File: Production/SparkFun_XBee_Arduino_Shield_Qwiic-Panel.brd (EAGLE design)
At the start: 120.9 x 213.4 mm, 1008 parts, among them J1 QWIIC_RIGHT_ANGLE, J13 QWIIC_RIGHT_ANGLE, J17 QWIIC_RIGHT_ANGLE, J21 QWIIC_RIGHT_ANGLE, J4 QWIIC_RIGHT_ANGLE, J9 QWIIC_RIGHT_ANGLE, Q1 220mA/50V/3.5Ω, Q11 3.1A/30V/105mΩ, Q12 220mA/50V/3.5Ω, Q13 20V/4.2A/52mΩ/1.4W, Q15 3.1A/30V/105mΩ, Q16 220mA/50V/3.5Ω, Q17 20V/4.2A/52mΩ/1.4W, Q19 3.1A/30V/105mΩ, Q2 20V/4.2A/52mΩ/1.4W, Q20 220mA/50V/3.5Ω, Q21 20V/4.2A/52mΩ/1.4W, Q23 3.1A/30V/105mΩ, Q24 220mA/50V/3.5Ω, Q3 3.1A/30V/105mΩ, Q5 20V/4.2A/52mΩ/1.4W, Q6 3.1A/30V/105mΩ, Q8 220mA/50V/3.5Ω, Q9 20V/4.2A/52mΩ/1.4W, U1 FSUSB30MUX_MSOP10, U10 FT231XS, U11 AP63203, U12 ESD Diode, U13 FSUSB30MUX_MSOP10, U14 ESD Diode, U15 FT231XS, U16 AP63203, U17 ESD Diode, U18 FSUSB30MUX_MSOP10, U19 ESD Diode, U2 AP63203, U20 FT231XS, U21 AP63203, U22 ESD Diode, U23 FSUSB30MUX_MSOP10, U24 ESD Diode, U25 FT231XS, U26 AP63203, U27 ESD Diode, U28 FSUSB30MUX_MSOP10, U29 ESD Diode, U3 ESD Diode, U30 FT231XS, U4 FT231XS, U5 ESD Diode, U6 AP63203, U7 ESD Diode, U8 FSUSB30MUX_MSOP10, U9 ESD Diode, X1 JUMPER-SMT_2_NO_SILK, X2 JUMPER-SMT_2_NO_SILK, X3 JUMPER-SMT_2_NO_SILK, X4 JUMPER-SMT_2_NO_SILK, X5 JUMPER-SMT_2_NO_SILK, X6 JUMPER-SMT_2_NO_SILK

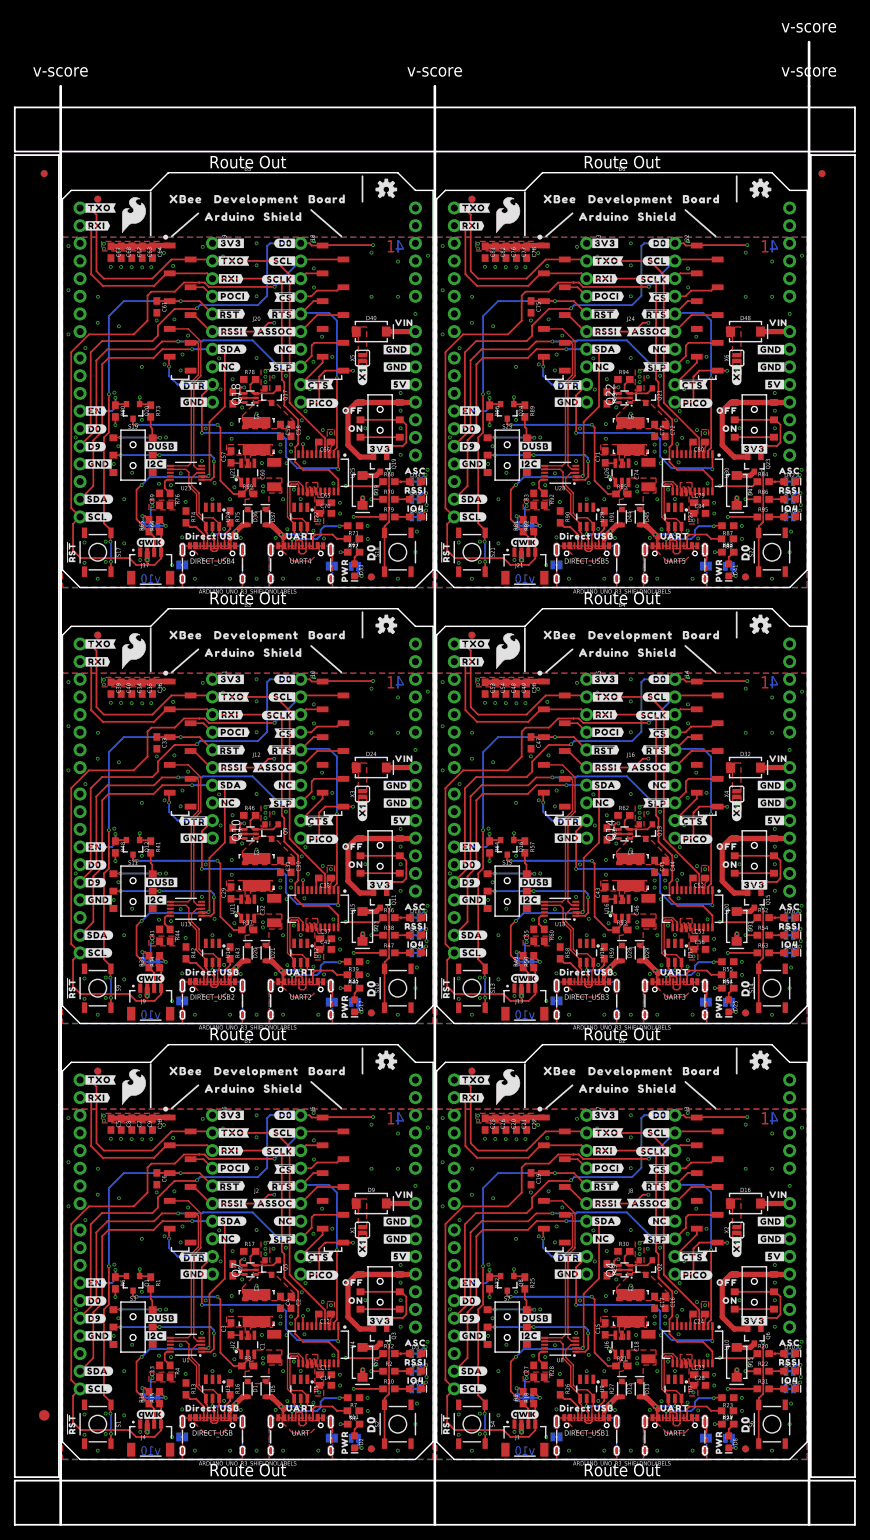
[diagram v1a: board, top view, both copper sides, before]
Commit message: Small adjustment to design file after approving proximity DRC error
* Remakes panels
* Deletes old library
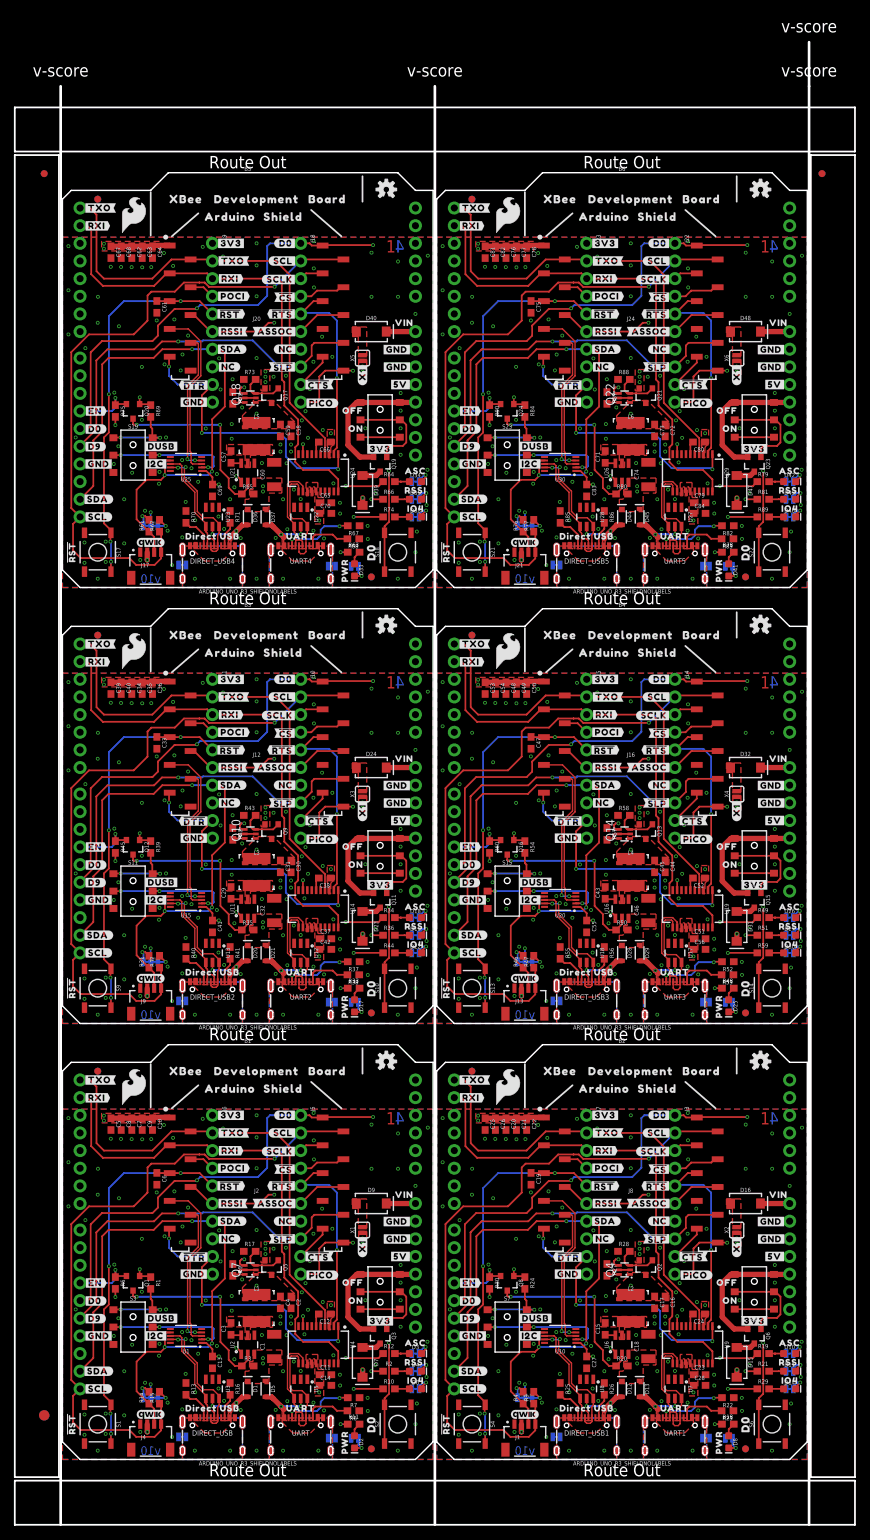
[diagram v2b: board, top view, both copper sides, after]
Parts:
- removed R91: 5.1k, SparkFun-Resistors:0603
- removed R92: 100, SparkFun-Resistors:0603
- removed R93: 100k, SparkFun-Resistors:0603
- removed R94: 1M, SparkFun-Resistors:0603
- removed R95: 330, SparkFun-Resistors:0603
- removed R96: 10k, SparkFun-Resistors:0603
- R18, R33: value 2.2k -> 4.7k
- R19, R51: value 4.7k -> 2.2k
- R20, R50, R54, R65, R84: value 2.2k -> 100k
- R21, R61, R77: value 100k -> 2.2k
- R22, R38, R52, R68, R70, R82, R86: value 2.2k -> 5.1k
- R24, R27, R39, R42, R72, R87: value 5.1k -> 100k
- R25, R37, R41, R53, R85: value 100k -> 5.1k
- R28: value 100 -> 1M
- R29, R89: value 100k -> 330
- R30: value 1M -> 10k
- R31, R47, R79: value 330 -> 2.2k
- R32, R64: value 10k -> 2.2k
- R35: value 4.7k -> 100k
- R4, R76: value 100 -> 2.2k
- R43, R58, R88: value 5.1k -> 1M
- R44: value 100 -> 330
- R45: value 100k -> 10k
- R46, R62: value 1M -> 2.2k
- R48: value 10k -> 4.7k
- R59, R74: value 5.1k -> 330
- R60: value 100 -> 10k
- R63: value 330 -> 4.7k
- R67, R83: value 4.7k -> 5.1k
- R73: value 100k -> 1M
- R75, R90: value 5.1k -> 10k
- R78: value 1M -> 4.7k
- R80: value 10k -> 100k
- U1: value FSUSB30MUX_MSOP10 -> FSUSB42MUX
- U10, U15, U20, U25, U30: value FT231XS -> FSUSB42MUX; device SparkFun-IC-Comms:SSOP20_L -> SparkFun-IC-Special-Function:MSOP10
- U13, U18, U23, U28, U8: value FSUSB30MUX_MSOP10 -> ESD Diode; device SparkFun-IC-Special-Function:MSOP10 -> SparkFun-DiscreteSemi:SOT-23-6
- U14, U19, U24, U29, U9: value ESD Diode -> FT231XS; device SparkFun-DiscreteSemi:SOT-23-6 -> SparkFun-IC-Comms:SSOP20_L
- moved R31 107.7 mm to (12.4, 71.6), turned to 90 degrees
- moved R48 90.5 mm to (95.8, 67.8), turned to 0 degrees
- moved R63 82.4 mm to (41.9, 130.6)
- moved R61 79.4 mm to (12.4, 134.4), turned to 90 degrees
- moved R62 78.8 mm to (14.0, 134.4), turned to 90 degrees
- moved R80 73.9 mm to (80.5, 138.9), turned to 0 degrees
- moved R78 73.2 mm to (95.8, 130.6)
- moved R32 66.3 mm to (14.0, 71.6), turned to 90 degrees
- moved R64 54.5 mm to (47.0, 140.7), turned to 0 degrees
- moved R79 54.1 mm to (100.8, 140.7)
- moved R4 50.9 mm to (66.3, 8.89), turned to 90 degrees
- moved R76 50.9 mm to (66.3, 134.4), turned to 90 degrees
- moved R77 47.0 mm to (67.8, 134.4), turned to 90 degrees
- moved R46 44.6 mm to (66.3, 71.6), turned to 90 degrees
- moved R89 37.5 mm to (100.8, 135.6), turned to 0 degrees
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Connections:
- removed net N$102 (its old number): DIRECT_USB4.A5, R74.2
- removed net N$103 (its old number): R76.1, U23.10
- removed net N$104 (its old number): Q18.2, Q18.5, Q18.6, R77.2
- removed net N$105 (its old number): Q17.1, Q18.3, R78.2
- removed net N$111 (its old number): I2C_PU5.3, R81.2
- removed net N$112 (its old number): I2C_PU5.1, R82.2
- removed net N$113 (its old number): D41.A, R83.2
- removed net N$123 (its old number): DIRECT_USB5.B5, R91.2
- removed net N$124 (its old number): DIRECT_USB5.A5, R90.2
- removed net N$125 (its old number): R92.1, U28.10
- removed net N$126 (its old number): Q22.2, Q22.5, Q22.6, R93.2
- removed net N$127: Q21.1, Q22.3, R94.2
- removed net N$128: D46.A, R95.2
- removed net N$25 (its old number): D10.A, R20.2
- removed net N$31 (its old number): D11.A, R22.2
- removed net N$39 (its old number): Q2.1, Q4.3, R30.2
- removed net N$40 (its old number): D14.A, R31.2
- removed net N$47 (its old number): D17.A, R35.2
- removed net N$48 (its old number): D18.A, R36.2
- removed net N$60 (its old number): Q10.2, Q10.5, Q10.6, R45.2
- removed net N$61 (its old number): Q10.3, Q9.1, R46.2
- removed net N$62 (its old number): D22.A, R47.2
- removed net N$68 (its old number): I2C_PU3.1, R50.2
- removed net N$69 (its old number): D25.A, R51.2
- removed net N$70 (its old number): D26.A, R52.2
- removed net N$81 (its old number): R60.1, U18.10
- removed net N$82 (its old number): Q14.2, Q14.5, Q14.6, R61.2
- removed net N$83 (its old number): Q13.1, Q14.3, R62.2
- removed net N$84 (its old number): D30.A, R63.2
- removed net N$89 (its old number): I2C_PU4.3, R65.2
- removed net N$90 (its old number): I2C_PU4.1, R66.2
- removed net N$91 (its old number): D33.A, R67.2
- removed net N$92 (its old number): D34.A, R68.2
- new net N$107: I2C_PU5.1, R77.2
- new net N$108: D41.A, R78.2
- new net N$109: D42.A, R79.2
- new net N$116: R83.2, UART5.B5
- new net N$117: R82.2, UART5.A5
- new net N$118: DIRECT_USB5.B5, R86.2
- new net N$120: Q22.2, Q22.5, Q22.6, R87.2
- new net N$30: D11.A, R21.2
- new net N$32: R23.2, UART1.B5
- new net N$43: I2C_PU2.3, R31.2
- new net N$44: I2C_PU2.1, R32.2
- new net N$51: D19.A, R36.2
- new net N$54: R37.2, UART2.A5
- new net N$64: I2C_PU3.3, R46.2
- new net N$65: I2C_PU3.1, R47.2
- new net N$66: D25.A, R48.2
- new net N$72: D27.A, R51.2
- new net N$74: R53.2, UART3.B5
- new net N$76: DIRECT_USB3.B5, R56.2
- new net N$85: I2C_PU4.3, R61.2
- new net N$86: I2C_PU4.1, R62.2
- new net N$87: D33.A, R63.2
- new net N$88: D34.A, R64.2
- new net N$93: D35.A, R66.2
- new net N$95: R68.2, UART4.B5
- new net N$96: R67.2, UART4.A5
- new net N$98: DIRECT_USB4.A5, R70.2
- net 3.3V: now also U1.1; no longer R4.2
- net 3.3V1: now also R18.1, R24.1, R30.2, U10.1, U9.13, U9.14, U9.15, U9.3; no longer R19.1, R25.1, R28.2, R32.2, U10.13, U10.14, U10.15, U10.3
- net 3.3V2: now also R33.1, R39.1, R45.2, U14.13, U14.14, U14.15, U14.3, U15.1; no longer R35.1, R41.1, R44.2, R48.2, U15.13, U15.14, U15.15, U15.3
- net 3.3V3: now also R48.1, R54.1, U19.13, U19.14, U19.15, U19.3, U20.1; no longer R51.1, R57.1, R64.2, U20.13, U20.14, U20.15, U20.3
- net 3.3V4: now also R63.1, R69.1, R75.2, U24.13, U24.14, U24.15, U24.3, U25.1; no longer R67.1, R73.1, R76.2, R80.2, U25.13, U25.14, U25.15, U25.3
- net 3.3V5: now also R78.1, R84.1, R90.2, U29.13, U29.14, U29.15, U29.3, U30.1; no longer R83.1, R89.1, R92.2, R96.2, U30.13, U30.14, U30.15, U30.3
- net D+1: now also U9.11; no longer U10.11
- net D+2: now also U14.11; no longer U15.11
- net D+3: now also U19.11; no longer U20.11
- net D+4: now also U24.11; no longer U25.11
- net D+5: now also U29.11; no longer U30.11
- net D-1: now also U9.12; no longer U10.12
- net D-2: now also U14.12; no longer U15.12
- net D-3: now also U19.12; no longer U20.12
- net D-4: now also U24.12; no longer U25.12
- net D-5: now also U29.12; no longer U30.12
- net D1/SCL1: now also R9.1; no longer R18.1
- net D1/SCL2: now also R32.1; no longer R34.1
- net D1/SCL3: now also R47.1; no longer R50.1
- net D1/SCL4: now also R62.1; no longer R66.1
- net D1/SCL5: now also R77.1; no longer R82.1
- net D10/RSSI_PWM1: now also R21.1; no longer R22.1
- net D10/RSSI_PWM2: now also R36.1; no longer R38.1
- net D10/RSSI_PWM3: now also R51.1; no longer R54.1
- net D10/RSSI_PWM4: now also R66.1; no longer R70.1
- net D10/RSSI_PWM5: now also R81.1; no longer R86.1
- net D11/SDA: now also U1.7; no longer U1.2
- net D11/SDA1: now also R4.1, U10.7; no longer R9.1, U8.2
- net D11/SDA2: now also R31.1, U15.7; no longer R33.1, U13.2
- net D11/SDA3: now also R46.1, U20.7; no longer R49.1, U18.2
- net D11/SDA4: now also R61.1, U25.7; no longer R65.1, U23.2
- net D11/SDA5: now also R76.1, U30.7; no longer R81.1, U28.2
- net D13/TXO1: now also U9.4; no longer U10.4
- net D13/TXO2: now also U14.4; no longer U15.4
- net D13/TXO3: now also U19.4; no longer U20.4
- net D13/TXO4: now also U24.4; no longer U25.4
- net D13/TXO5: now also U29.4; no longer U30.4
- net D14/RXI1: now also U9.20; no longer U10.20
- net D14/RXI2: now also U14.20; no longer U15.20
- net D14/RXI3: now also U19.20; no longer U20.20
- net D14/RXI4: now also U24.20; no longer U25.20
- net D14/RXI5: now also U29.20; no longer U30.20
- net D4/SPI_PICO1: now also R29.1; no longer R31.1
- net D4/SPI_PICO2: now also R44.1; no longer R47.1
- net D4/SPI_PICO3: now also R59.1; no longer R63.1
- net D4/SPI_PICO4: now also R74.1; no longer R79.1
- net D4/SPI_PICO5: now also R89.1; no longer R95.1
- net D5/ASSOCIATE1: now also R19.1; no longer R20.1
- net D5/ASSOCIATE2: now also R34.1; no longer R36.1
- net D5/ASSOCIATE3: now also R49.1; no longer R52.1
- net D5/ASSOCIATE4: now also R64.1; no longer R68.1
- net D5/ASSOCIATE5: now also R79.1; no longer R84.1
- net D6/!RTS!1: now also U9.2; no longer U10.2
- net D6/!RTS!2: now also U14.2; no longer U15.2
- net D6/!RTS!3: now also U19.2; no longer U20.2
- net D6/!RTS!4: now also U24.2; no longer U25.2
- net D6/!RTS!5: now also U29.2; no longer U30.2
- net D7/!CTS!1: now also U9.9; no longer U10.9
- net D7/!CTS!2: now also U14.9; no longer U15.9
- net D7/!CTS!3: now also U19.9; no longer U20.9
- net D7/!CTS!4: now also U24.9; no longer U25.9
- net D7/!CTS!5: now also U29.9; no longer U30.9
- net D8/!DTR!1: now also U9.1; no longer U10.1
- net D8/!DTR!2: now also U14.1; no longer U15.1
- net D8/!DTR!3: now also U19.1; no longer U20.1
- net D8/!DTR!4: now also U24.1; no longer U25.1
- net D8/!DTR!5: now also U29.1; no longer U30.1
- net DIRECT_D+: now also U1.9; no longer U1.3
- net DIRECT_D+1: now also U10.9, U8.6; no longer U8.3, U9.6
- net DIRECT_D+2: now also U13.6, U15.9; no longer U13.3, U14.6
- net DIRECT_D+3: now also U18.6, U20.9; no longer U18.3, U19.6
- net DIRECT_D+4: now also U23.6, U25.9; no longer U23.3, U24.6
- net DIRECT_D+5: now also U28.6, U30.9; no longer U28.3, U29.6
- net DIRECT_D-: now also U1.8; no longer U1.7
- net DIRECT_D-1: now also U10.8, U8.4; no longer U8.7, U9.4
- net DIRECT_D-2: now also U13.4, U15.8; no longer U13.7, U14.4
- net DIRECT_D-3: now also U18.4, U20.8; no longer U18.7, U19.4
- net DIRECT_D-4: now also U23.4, U25.8; no longer U23.7, U24.4
- net DIRECT_D-5: now also U28.4, U30.8; no longer U28.7, U29.4
- net DIRECT_SELECT: now also U1.2; no longer U1.1
- net DIRECT_SELECT1: now also U10.2; no longer U8.1
- net DIRECT_SELECT2: now also U15.2; no longer U13.1
- net DIRECT_SELECT3: now also U20.2; no longer U18.1
- net DIRECT_SELECT4: now also U25.2; no longer U23.1
- net DIRECT_SELECT5: now also U30.2; no longer U28.1
- net DIRECT_USB1: now also R24.2; no longer R25.2
- net DIRECT_USB2: now also R39.2; no longer R41.2
- net DIRECT_USB3: now also R54.2; no longer R57.2
- net DIRECT_USB4: now also R69.2; no longer R73.2
- net DIRECT_USB5: now also R84.2; no longer R89.2
- net EN-TRANS1: now also R30.1; no longer R32.1
- net EN-TRANS2: now also R45.1; no longer R48.1
- net EN-TRANS3: now also R60.1; no longer R64.1
- net EN-TRANS4: now also R75.1; no longer R80.1
- net EN-TRANS5: now also R90.1; no longer R96.1
- net EN1: now also R20.1; no longer R21.1
- net EN2: now also R35.1; no longer R37.1
- net EN3: now also R50.1; no longer R53.1
- net EN4: now also R65.1; no longer R69.1
- net EN5: now also R80.1; no longer R85.1
- net GND: now also U1.10; no longer U1.9
- net GND1: now also R22.1, R25.1, R28.1, U10.10, U10.5, U8.2, U9.16, U9.6; no longer R24.1, R29.1, R30.1, U10.16, U10.6, U8.5, U8.9, U9.2
- net GND2: now also R37.1, R38.1, R41.1, U13.2, U14.16, U14.6, U15.10, U15.5; no longer R39.1, R45.1, R46.1, U13.5, U13.9, U14.2, U15.16, U15.6
- net GND3: now also R52.1, R53.1, R57.1, U18.2, U19.16, U19.6, U20.10, U20.5; no longer R59.1, R61.1, R62.1, U18.5, U18.9, U19.2, U20.16, U20.6
- net GND4: now also R67.1, R68.1, R70.1, R73.1, U23.2, U24.16, U24.6, U25.10, U25.5; no longer R74.1, R75.1, R77.1, R78.1, U23.5, U23.9, U24.2, U25.16, U25.6
- net GND5: now also R82.1, R83.1, R85.1, R86.1, U28.2, U29.16, U29.6, U30.10, U30.5; no longer R90.1, R91.1, R93.1, R94.1, U28.5, U28.9, U29.2, U30.16, U30.6
- net N$10: now also I2C_PU1.3, R4.2; no longer R4.1, U1.10
- net N$100: now also Q17.1, Q18.3, R73.2; no longer R71.2, UART4.A5
- net N$101: now also D38.A, R74.2; no longer DIRECT_USB4.B5, R75.2
- net N$106: now also I2C_PU5.3, R76.2; no longer D38.A, R79.2
- net N$114: now also D43.A, R81.2; no longer D42.A, R84.2
- net N$119: now also DIRECT_USB5.A5, R85.2; no longer D43.A, R86.2
- net N$121: now also Q21.1, Q22.3; no longer UART5.B5
- net N$122: now also D46.A, R89.2; no longer R87.2, UART5.A5
- net N$18: now also I2C_PU1.1; no longer I2C_PU1.3
- net N$22: now also D8.A; no longer I2C_PU1.1
- net N$24: now also D10.A; no longer D8.A
- net N$33: now also R22.2, UART1.A5; no longer R24.2, UART1.B5
- net N$34: now also DIRECT_USB1.B5, R26.2; no longer R23.2, UART1.A5
- net N$35: now also DIRECT_USB1.A5, R25.2; no longer DIRECT_USB1.B5, R27.2
- net N$36: now also Q4.2, Q4.5, Q4.6, R27.2; no longer DIRECT_USB1.A5, R26.2
- net N$37: now also Q2.1, Q4.3, R28.2; no longer R28.1, U8.10
- net N$38: now also D14.A; no longer Q4.2, Q4.5, Q4.6
- net N$45: now also D17.A; no longer I2C_PU2.3
- net N$46: now also D18.A; no longer I2C_PU2.1
- net N$53: now also UART2.B5; no longer D19.A
- net N$55: now also DIRECT_USB2.B5, R41.2; no longer R40.2, UART2.B5
- net N$56: now also DIRECT_USB2.A5, R40.2; no longer R39.2, UART2.A5
- net N$57: now also Q10.2, Q10.5, Q10.6, R42.2; no longer DIRECT_USB2.B5, R43.2
- net N$58: now also Q10.3, Q9.1, R43.2; no longer DIRECT_USB2.A5, R42.2
- net N$59: now also D22.A, R44.2; no longer R44.1, U13.10
- net N$67: now also D26.A; no longer I2C_PU3.3
- net N$75: now also R52.2, UART3.A5; no longer D27.A, R54.2
- net N$77: now also DIRECT_USB3.A5, R55.2; no longer R56.2, UART3.B5
- net N$78: now also Q14.2, Q14.5, Q14.6, R57.2; no longer R55.2, UART3.A5
- net N$79: now also Q13.1, Q14.3, R58.2; no longer DIRECT_USB3.B5, R59.2
- net N$80: now also D30.A, R59.2; no longer DIRECT_USB3.A5, R58.2
- net N$97: now also DIRECT_USB4.B5, R71.2; no longer D35.A, R70.2
- net N$99: now also Q18.2, Q18.5, Q18.6; no longer UART4.B5
- net VCC1: now also R20.2; no longer R21.2
- net VCC2: now also R35.2; no longer R37.2
- net VCC3: now also R50.2; no longer R53.2
- net VCC4: now also R65.2; no longer R69.2
- net VCC5: now also R80.2; no longer R85.2
- net V_USB_1: now also U8.5; no longer U9.5
- net V_USB_3: now also U13.5; no longer U14.5
- net V_USB_4: now also U18.5; no longer U19.5
- net V_USB_5: now also U23.5; no longer U24.5
- net V_USB_6: now also U28.5; no longer U29.5
- net XBEE_D+/SDA: now also U1.3; no longer U1.4
- net XBEE_D+/SDA1: now also U10.3; no longer U8.4
- net XBEE_D+/SDA2: now also U15.3; no longer U13.4
- net XBEE_D+/SDA3: now also U20.3; no longer U18.4
- net XBEE_D+/SDA4: now also U25.3; no longer U23.4
- net XBEE_D+/SDA5: now also U30.3; no longer U28.4
- net XBEE_D-: now also U1.4; no longer U1.6
- net XBEE_D-1: now also U10.4; no longer U8.6
- net XBEE_D-2: now also U15.4; no longer U13.6
- net XBEE_D-3: now also U20.4; no longer U18.6
- net XBEE_D-4: now also U25.4; no longer U23.6
- net XBEE_D-5: now also U30.4; no longer U28.6
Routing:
- net N$117: track 0.00 -> 10.3 mm, vias 0 -> 2
- net N$96: track 0.00 -> 10.3 mm, vias 0 -> 2
- net N$54: track 0.00 -> 10.3 mm, vias 0 -> 2
- net N$122: track 10.3 -> 2.08 mm, vias 2 -> 0
- net N$75: track 2.08 -> 10.3 mm, vias 0 -> 2
- net N$116: track 0.00 -> 6.64 mm
- net N$95: track 0.00 -> 6.64 mm
- net N$32: track 0.00 -> 6.64 mm
- net N$74: track 0.00 -> 6.64 mm
- net N$34: track 10.3 -> 3.63 mm, vias 2 -> 0
- net N$83 (its old number): track 6.41 -> 0.00 mm
- net N$61 (its old number): track 6.41 -> 0.00 mm
- net N$39 (its old number): track 6.41 -> 0.00 mm
- net N$127: track 6.41 -> 0.00 mm
- net N$105 (its old number): track 6.41 -> 0.00 mm
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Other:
- board text added: "Material: FR4: TG135-140"
- board text added: "Red Soldermask"
- board text added: "White Silk"

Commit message: Adds new v11 panel
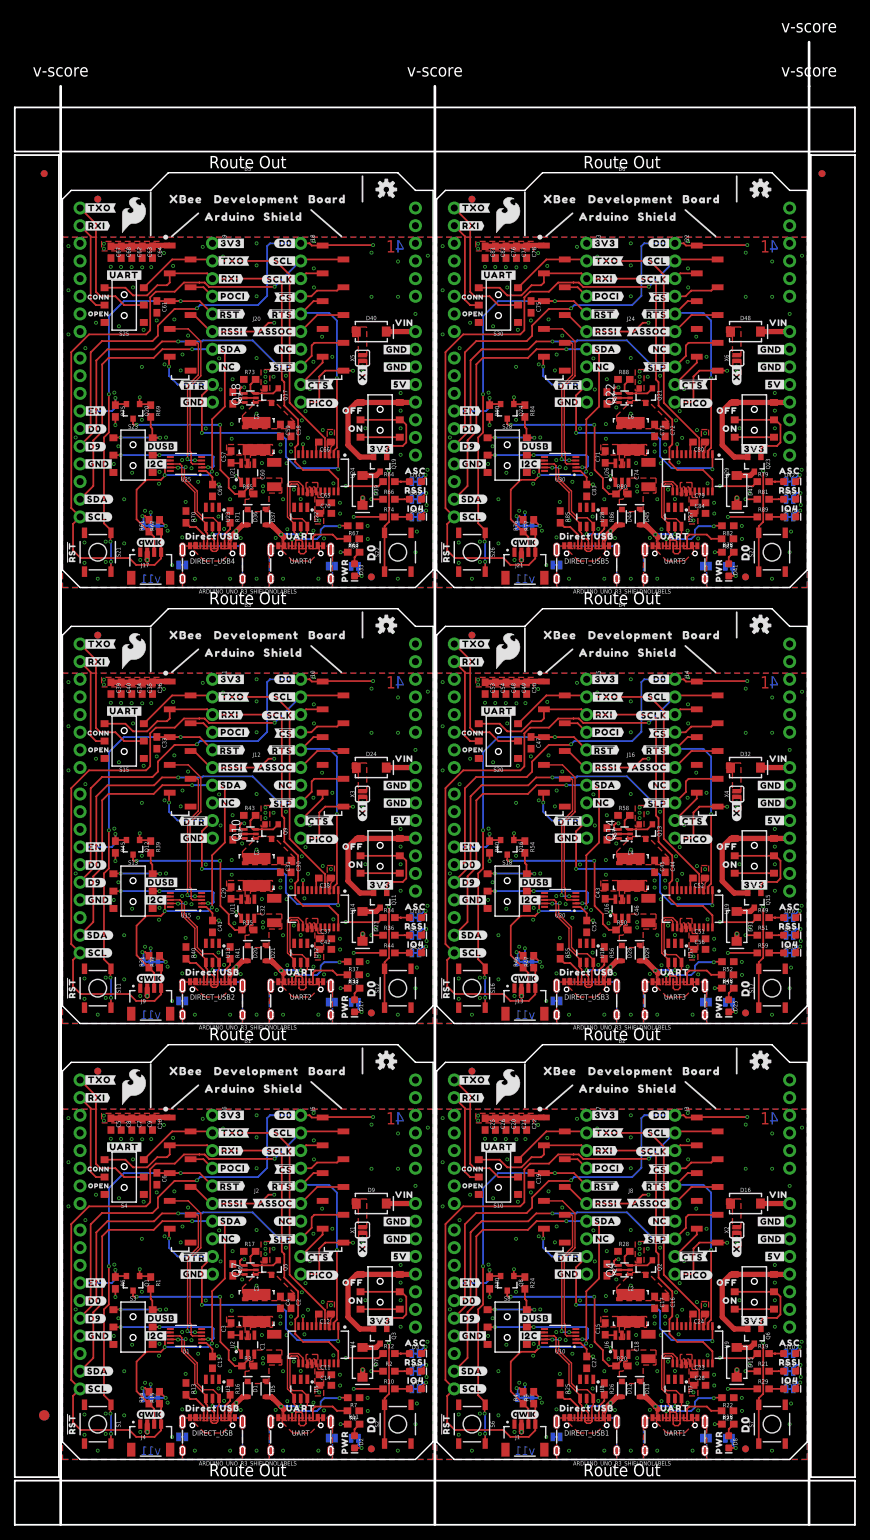
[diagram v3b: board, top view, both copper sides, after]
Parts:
- removed LOGO19, LOGO23: SFE_LOGO_NAMEBLANK, SparkFun-Aesthetics:BLANK
- removed LOGO20, LOGO24: SPECIAL_INSTRUCTIONS-ORDERING, SparkFun-Aesthetics:ORDERING_INSTRUCTIONS
- removed LOGO21: OSHW-LOGOS, SparkFun-Aesthetics:OSHW-LOGO-S
- removed LOGO22: QWIIC_LOGO_4MM, SparkFun-Aesthetics:QWIIC_4MM
- added S25, S28, S29, S30: (no value), SparkFun-Switches:SWITCH_DPDT_SMD_AYZ0202
- added S26, S27: (no value), SparkFun-Switches:TACTILE_SWITCH_SMD_5.2MM
- added U$553: (no value), bot:#D0#3
- added U$554: (no value), bot:#X1#10
- added U$555: (no value), bot:ON38
- added U$556, U$557, U$561: (no value), topmirror:#GND#0
- added U$558: (no value), topmirror:#5V#5
- added U$559: (no value), top:#SDA#9
- added U$560: (no value), bot:#SCL#13
- added U$562: (no value), botmirror:#EN#15
- added U$563: (no value), top:#3V3#1
- added U$564: (no value), botmirror:##RST##13
- added U$565: (no value), topmirror:#VIN#4
- added U$566: (no value), pot:#D0#3416
- added U$567: (no value), pot:#D9#3416
- added U$568: (no value), top:#UART#4048234
- added U$569: (no value), top:CONN4048235
- added U$570: (no value), top:OPEN4048238
- LOGO10: value QWIIC_LOGO_4MM -> OSHW-LOGOS; device SparkFun-Aesthetics:QWIIC_4MM -> SparkFun-Aesthetics:OSHW-LOGO-S
- LOGO11: value SFE_LOGO_NAMEBLANK -> QWIIC_LOGO_4MM; device SparkFun-Aesthetics:BLANK -> SparkFun-Aesthetics:QWIIC_4MM
- LOGO12: value SPECIAL_INSTRUCTIONS-ORDERING -> SFE_LOGO_NAMEBLANK; device SparkFun-Aesthetics:ORDERING_INSTRUCTIONS -> SparkFun-Aesthetics:BLANK
- LOGO16, LOGO4: value SPECIAL_INSTRUCTIONS-ORDERING -> OSHW-LOGOS; device SparkFun-Aesthetics:ORDERING_INSTRUCTIONS -> SparkFun-Aesthetics:OSHW-LOGO-S
- LOGO17, LOGO5: value OSHW-LOGOS -> QWIIC_LOGO_4MM; device SparkFun-Aesthetics:OSHW-LOGO-S -> SparkFun-Aesthetics:QWIIC_4MM
- LOGO18, LOGO6: value QWIIC_LOGO_4MM -> SFE_LOGO_NAMEBLANK; device SparkFun-Aesthetics:QWIIC_4MM -> SparkFun-Aesthetics:BLANK
- LOGO7: value SFE_LOGO_NAMEBLANK -> OSHW-LOGOS; device SparkFun-Aesthetics:BLANK -> SparkFun-Aesthetics:OSHW-LOGO-S
- LOGO8: value SPECIAL_INSTRUCTIONS-ORDERING -> QWIIC_LOGO_4MM; device SparkFun-Aesthetics:ORDERING_INSTRUCTIONS -> SparkFun-Aesthetics:QWIIC_4MM
- LOGO9: value OSHW-LOGOS -> SFE_LOGO_NAMEBLANK; device SparkFun-Aesthetics:OSHW-LOGO-S -> SparkFun-Aesthetics:BLANK
- S10, S13, S14, S18, S4, S9: device SparkFun-Switches:TACTILE_SWITCH_SMD_5.2MM -> SparkFun-Switches:SWITCH_DPDT_SMD_AYZ0202
- S11, S12, S16, S7: device SparkFun-Switches:SWITCH_DPDT_SMD_AYZ0202 -> SparkFun-Switches:TACTILE_SWITCH_SMD_5.2MM
- U$100: device topmirror:#D6##RTS##25 -> topmirror:#D1#AD1#8
- U$101: device topmirror:#D5#ASSOC#25 -> topmirror:#D2#AD2#19
- U$102: device topmirror:#D9##SLP##28 -> topmirror:#D3#AD3#23
- U$103: device topmirror:#D7##CTS##26 -> topmirror:#D6##RTS##25
- U$104: device topmirror:#D4#PICO#25 -> topmirror:#D5#ASSOC#25
- U$105: device topmirror:#D8##DTR##27 -> topmirror:#D9##SLP##28
- U$106: device topmirror:#RSSI#D10#17 -> topmirror:#D7##CTS##26
- U$107: device topmirror:#SDA#D11#9 -> topmirror:#D4#PICO#25
- U$108: device topmirror:##RST##15 -> topmirror:#D8##DTR##27
- U$109: device topmirror:#POCI#D12#24 -> topmirror:#RSSI#D10#17
- U$110: device topmirror:#RXI#D14#15 -> topmirror:#SDA#D11#9
- U$111: device topmirror:#TXO#D13#13 -> topmirror:##RST##15
- U$112: device topmirror:#EN#17 -> topmirror:#POCI#D12#24
- U$113: device topmirror:#ALED#21 -> topmirror:#RXI#D14#15
- U$114: device topmirror:#RLED#22 -> topmirror:#TXO#D13#13
- U$115: device botmirror:#TXO#8 -> topmirror:#EN#17
- U$116: device botmirror:#RXI#7 -> topmirror:#ALED#21
- U$117: device botmirror:#POCI#32 -> topmirror:#RLED#22
- U$118: device botmirror:##RST##13 -> botmirror:#TXO#8
- U$119: device topmirror:#RSSI#16 -> botmirror:#RXI#7
- U$120: device botmirror:#SDA#10 -> botmirror:#POCI#32
- U$121: device botmirror:#ASSOC#28 -> botmirror:##RST##13
- U$122: device botmirror:##RTS##14 -> topmirror:#RSSI#16
- U$123: device botmirror:##CS##26 -> botmirror:#SDA#10
- U$124: device botmirror:#SCLK#33 -> botmirror:#ASSOC#28
- U$125: device botmirror:#SCL#9 -> botmirror:##RTS##14
- U$126: device botmirror:#D0#3 -> botmirror:##CS##26
- U$127: device topmirror:#SHLD#36 -> botmirror:#SCLK#33
- U$128: device topmirror:#NC#1 -> botmirror:#SCL#9
- U$129: device botmirror:#NC#3 -> botmirror:#D0#3
- U$130: device botmirror:#NC#3 -> topmirror:#SHLD#36
- U$131: device topmirror:UART34 -> topmirror:#NC#1
- U$132, U$228: device topmirror:#GND#0 -> botmirror:#NC#3
- U$133: device topmirror:#NC#1 -> botmirror:#NC#3
- U$134: device botmirror:#SDA#10 -> topmirror:UART34
- U$135: device top:#SCL#7 -> topmirror:#GND#0
- U$136, U$416: device topmirror:#GND#0 -> topmirror:#NC#1
- U$137: device botmirror:#TXO#8 -> botmirror:#SDA#10
- U$138: device botmirror:#RXI#7 -> top:#SCL#7
- U$139, U$272: device top:#3V3#1 -> topmirror:#GND#0
- U$140, U$425: device topmirror:#GND#0 -> botmirror:#TXO#8
- U$141: device SparkFun-Aesthetics:SFE_LOGO_NAME_.2 -> botmirror:#RXI#7
- U$142: device top:##SLP##28 -> top:#3V3#1
- U$143: device topmirror:DIRECT_USB33 -> topmirror:#GND#0
- U$144: device botmirror:#DUSB#31 -> SparkFun-Aesthetics:SFE_LOGO_NAME_.2
- U$145: device top:ASC32 -> top:##SLP##28
- U$146: device top:RSSI31 -> topmirror:DIRECT_USB33
- U$147: device top:PWR29 -> botmirror:#DUSB#31
- U$148: device topmirror:#SHLD1#37 -> top:ASC32
- U$149, U$529: device topmirror:#GND#0 -> top:RSSI31
- U$150, U$530: device top:#3V3#1 -> top:PWR29
- U$151: device topmirror:#D0#AD0#18 -> topmirror:#SHLD1#37
- U$152, U$428: device top:ARDUINO1345 -> topmirror:#GND#0
- U$153: device top:XBEE340 -> top:#3V3#1
- U$154: device top:SHIELD1346 -> topmirror:#D0#AD0#18
- U$155: device topmirror:#5V#5 -> top:ARDUINO1345
- U$156: device topmirror:DEVELOPMENT1346 -> top:XBEE340
- U$157: device topmirror:BOARD1347 -> top:SHIELD1346
- U$158: device top:#I2C#13751 -> topmirror:#5V#5
- U$159: device topmirror:##DTR##27 -> topmirror:DEVELOPMENT1346
- U$160: device top:##CTS##28 -> topmirror:BOARD1347
- U$161, U$541: device topmirror:#GND#0 -> top:#I2C#13751
- U$162: device top:#3V3#1 -> topmirror:##DTR##27
- U$163: device pot:OFF311 -> top:##CTS##28
- U$164, U$532: device top:#PLED#20 -> topmirror:#GND#0
- U$165, U$533: device pot:#IOLED#5 -> top:#3V3#1
- U$166: device pot:IO49 -> pot:OFF311
- U$167: device top:VIN5 -> top:#PLED#20
- U$168: device bot:#PICO#27 -> pot:#IOLED#5
- U$169: device bot:#D9#6 -> pot:IO49
- U$170: device bot:#D0#3 -> top:VIN5
- U$171: device bot:#X1#10 -> bot:#PICO#27
- U$172: device bot:ON38 -> bot:#D9#6
- U$173: device topmirror:#GND#0 -> bot:#D0#3
- U$174: device topmirror:#GND#0 -> bot:#X1#10
- U$175: device topmirror:#5V#5 -> bot:ON38
- U$176, U$544: device top:#SDA#9 -> topmirror:#GND#0
- U$177: device bot:#SCL#13 -> topmirror:#GND#0
- U$178, U$253: device topmirror:#GND#0 -> topmirror:#5V#5
- U$179: device botmirror:#EN#15 -> top:#SDA#9
- U$180: device top:#3V3#1 -> bot:#SCL#13
- U$181: device botmirror:##RST##13 -> topmirror:#GND#0
- U$182: device topmirror:#VIN#4 -> botmirror:#EN#15
- U$183: device pot:#D0#3416 -> top:#3V3#1
- U$184: device pot:#D9#3416 -> botmirror:##RST##13
- U$185: device top:#I2C#33 -> topmirror:#VIN#4
- U$186: device bot:D03 -> pot:#D0#3416
- U$187: device top:#RST#30 -> pot:#D9#3416
- U$188: device SparkFun-Aesthetics:SFE_LOGO_FLAME_.2 -> top:#UART#4048234
- U$189: device topmirror:#D1#AD1#8 -> top:CONN4048235
- U$190: device topmirror:#D2#AD2#19 -> top:OPEN4048238
- U$191: device topmirror:#D3#AD3#23 -> top:#I2C#33
- U$192: device topmirror:#D6##RTS##25 -> bot:D03
- U$193: device topmirror:#D5#ASSOC#25 -> top:#RST#30
- U$194: device topmirror:#D9##SLP##28 -> SparkFun-Aesthetics:SFE_LOGO_FLAME_.2
- U$195: device topmirror:#D7##CTS##26 -> topmirror:#D1#AD1#8
- U$196: device topmirror:#D4#PICO#25 -> topmirror:#D2#AD2#19
- U$197: device topmirror:#D8##DTR##27 -> topmirror:#D3#AD3#23
- U$198: device topmirror:#RSSI#D10#17 -> topmirror:#D6##RTS##25
- U$199: device topmirror:#SDA#D11#9 -> topmirror:#D5#ASSOC#25
- U$200: device topmirror:##RST##15 -> topmirror:#D9##SLP##28
- U$201: device topmirror:#POCI#D12#24 -> topmirror:#D7##CTS##26
- U$202: device topmirror:#RXI#D14#15 -> topmirror:#D4#PICO#25
- U$203: device topmirror:#TXO#D13#13 -> topmirror:#D8##DTR##27
- U$204: device topmirror:#EN#17 -> topmirror:#RSSI#D10#17
- U$205: device topmirror:#ALED#21 -> topmirror:#SDA#D11#9
- U$206: device topmirror:#RLED#22 -> topmirror:##RST##15
- U$207: device botmirror:#TXO#8 -> topmirror:#POCI#D12#24
- U$208: device botmirror:#RXI#7 -> topmirror:#RXI#D14#15
- U$209: device botmirror:#POCI#32 -> topmirror:#TXO#D13#13
- U$210: device botmirror:##RST##13 -> topmirror:#EN#17
- U$211: device topmirror:#RSSI#16 -> topmirror:#ALED#21
- U$212: device botmirror:#SDA#10 -> topmirror:#RLED#22
- U$213: device botmirror:#ASSOC#28 -> botmirror:#TXO#8
- U$214: device botmirror:##RTS##14 -> botmirror:#RXI#7
- U$215: device botmirror:##CS##26 -> botmirror:#POCI#32
- U$216: device botmirror:#SCLK#33 -> botmirror:##RST##13
- U$217: device botmirror:#SCL#9 -> topmirror:#RSSI#16
- U$218: device botmirror:#D0#3 -> botmirror:#SDA#10
- U$219: device topmirror:#SHLD#36 -> botmirror:#ASSOC#28
- U$220: device topmirror:#NC#1 -> botmirror:##RTS##14
- U$221: device botmirror:#NC#3 -> botmirror:##CS##26
- U$222: device botmirror:#NC#3 -> botmirror:#SCLK#33
- U$223: device topmirror:UART34 -> botmirror:#SCL#9
- U$224: device topmirror:#GND#0 -> botmirror:#D0#3
- U$225: device topmirror:#NC#1 -> topmirror:#SHLD#36
- U$226: device botmirror:#SDA#10 -> topmirror:#NC#1
- U$227: device top:#SCL#7 -> botmirror:#NC#3
- U$229: device botmirror:#TXO#8 -> topmirror:UART34
- U$230: device botmirror:#RXI#7 -> topmirror:#GND#0
- U$231: device top:#3V3#1 -> topmirror:#NC#1
- U$232, U$408, U$517: device topmirror:#GND#0 -> botmirror:#SDA#10
- U$233: device SparkFun-Aesthetics:SFE_LOGO_NAME_.2 -> top:#SCL#7
- U$234: device top:##SLP##28 -> topmirror:#GND#0
- U$235: device topmirror:DIRECT_USB33 -> botmirror:#TXO#8
- U$236: device botmirror:#DUSB#31 -> botmirror:#RXI#7
- U$237: device top:ASC32 -> top:#3V3#1
- U$238: device top:RSSI31 -> topmirror:#GND#0
- U$239: device top:PWR29 -> SparkFun-Aesthetics:SFE_LOGO_NAME_.2
- U$240: device topmirror:#SHLD1#37 -> top:##SLP##28
- U$241: device topmirror:#GND#0 -> topmirror:DIRECT_USB33
- U$242: device top:#3V3#1 -> botmirror:#DUSB#31
- U$243: device topmirror:#D0#AD0#18 -> top:ASC32
- U$244: device top:ARDUINO1345 -> top:RSSI31
- U$245: device top:XBEE340 -> top:PWR29
- U$246: device top:SHIELD1346 -> topmirror:#SHLD1#37
- U$247, U$523: device topmirror:#5V#5 -> topmirror:#GND#0
- U$248: device topmirror:DEVELOPMENT1346 -> top:#3V3#1
- U$249: device topmirror:BOARD1347 -> topmirror:#D0#AD0#18
- U$250: device top:#I2C#13751 -> top:ARDUINO1345
- U$251: device topmirror:##DTR##27 -> top:XBEE340
- U$252: device top:##CTS##28 -> top:SHIELD1346
- U$254: device top:#3V3#1 -> topmirror:DEVELOPMENT1346
- U$255: device pot:OFF311 -> topmirror:BOARD1347
- U$256: device top:#PLED#20 -> top:#I2C#13751
- U$257: device pot:#IOLED#5 -> topmirror:##DTR##27
- U$258: device pot:IO49 -> top:##CTS##28
- U$259: device top:VIN5 -> topmirror:#GND#0
- U$260: device bot:#PICO#27 -> top:#3V3#1
- U$261: device bot:#D9#6 -> pot:OFF311
- U$262: device bot:#D0#3 -> top:#PLED#20
- U$263: device bot:#X1#10 -> pot:#IOLED#5
- U$264: device bot:ON38 -> pot:IO49
- U$265: device topmirror:#GND#0 -> top:VIN5
- U$266: device topmirror:#GND#0 -> bot:#PICO#27
- U$267: device topmirror:#5V#5 -> bot:#D9#6
- U$268: device top:#SDA#9 -> bot:#D0#3
- U$269: device bot:#SCL#13 -> bot:#X1#10
- U$270: device topmirror:#GND#0 -> bot:ON38
- U$271: device botmirror:#EN#15 -> topmirror:#GND#0
- U$273: device botmirror:##RST##13 -> topmirror:#5V#5
- U$274: device topmirror:#VIN#4 -> top:#SDA#9
- U$275: device pot:#D0#3416 -> bot:#SCL#13
- U$276: device pot:#D9#3416 -> topmirror:#GND#0
- U$277: device top:#I2C#33 -> botmirror:#EN#15
- U$278: device bot:D03 -> top:#3V3#1
- U$279: device top:#RST#30 -> botmirror:##RST##13
- U$280: device SparkFun-Aesthetics:SFE_LOGO_FLAME_.2 -> topmirror:#VIN#4
- U$281: device topmirror:#D1#AD1#8 -> pot:#D0#3416
- U$282: device topmirror:#D2#AD2#19 -> pot:#D9#3416
- U$283: device topmirror:#D3#AD3#23 -> top:#UART#4048234
- U$284: device topmirror:#D6##RTS##25 -> top:CONN4048235
- U$285: device topmirror:#D5#ASSOC#25 -> top:OPEN4048238
- U$286: device topmirror:#D9##SLP##28 -> top:#I2C#33
- U$287: device topmirror:#D7##CTS##26 -> bot:D03
- U$288: device topmirror:#D4#PICO#25 -> top:#RST#30
- U$289: device topmirror:#D8##DTR##27 -> SparkFun-Aesthetics:SFE_LOGO_FLAME_.2
- U$290: device topmirror:#RSSI#D10#17 -> topmirror:#D1#AD1#8
- U$291: device topmirror:#SDA#D11#9 -> topmirror:#D2#AD2#19
- U$292: device topmirror:##RST##15 -> topmirror:#D3#AD3#23
- U$293: device topmirror:#POCI#D12#24 -> topmirror:#D6##RTS##25
- U$294: device topmirror:#RXI#D14#15 -> topmirror:#D5#ASSOC#25
- U$295: device topmirror:#TXO#D13#13 -> topmirror:#D9##SLP##28
- U$296: device topmirror:#EN#17 -> topmirror:#D7##CTS##26
- U$297: device topmirror:#ALED#21 -> topmirror:#D4#PICO#25
- U$298: device topmirror:#RLED#22 -> topmirror:#D8##DTR##27
- U$299: device botmirror:#TXO#8 -> topmirror:#RSSI#D10#17
- U$300: device botmirror:#RXI#7 -> topmirror:#SDA#D11#9
- U$301: device botmirror:#POCI#32 -> topmirror:##RST##15
- U$302: device botmirror:##RST##13 -> topmirror:#POCI#D12#24
- U$303: device topmirror:#RSSI#16 -> topmirror:#RXI#D14#15
- U$304: device botmirror:#SDA#10 -> topmirror:#TXO#D13#13
- U$305: device botmirror:#ASSOC#28 -> topmirror:#EN#17
- U$306: device botmirror:##RTS##14 -> topmirror:#ALED#21
- U$307: device botmirror:##CS##26 -> topmirror:#RLED#22
- U$308: device botmirror:#SCLK#33 -> botmirror:#TXO#8
- U$309: device botmirror:#SCL#9 -> botmirror:#RXI#7
- U$310: device botmirror:#D0#3 -> botmirror:#POCI#32
- U$311: device topmirror:#SHLD#36 -> botmirror:##RST##13
- U$312: device topmirror:#NC#1 -> topmirror:#RSSI#16
- U$313: device botmirror:#NC#3 -> botmirror:#SDA#10
- U$314: device botmirror:#NC#3 -> botmirror:#ASSOC#28
- U$315: device topmirror:UART34 -> botmirror:##RTS##14
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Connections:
- new net D13/TXO-R1: B2.RX, S10.5
- new net D13/TXO-R2: B3.RX, S15.5
- new net D13/TXO-R3: B1.RX, S4.5
- new net D13/TXO-R4: B4.RX, S20.5
- new net D13/TXO-R5: B5.RX, S25.5
- new net D13/TXO-R6: B6.RX, S30.5
- new net D14/RXI-R1: B2.TX, S10.2
- new net D14/RXI-R2: B3.TX, S15.2
- new net D14/RXI-R3: B1.TX, S4.2
- new net D14/RXI-R4: B4.TX, S20.2
- new net D14/RXI-R5: B5.TX, S25.2
- new net D14/RXI-R6: B6.TX, S30.2
- net !RESET!1: now also S6.1, S6.2; no longer S4.1, S4.2
- net !RESET!2: now also S11.1, S11.2; no longer S9.1, S9.2
- net !RESET!3: now also S16.1, S16.2; no longer S13.1, S13.2
- net !RESET!4: now also S21.1, S21.2; no longer S17.1, S17.2
- net !RESET!5: now also S26.1, S26.2; no longer S21.1, S21.2
- net 3.3V_SW1: now also S9.3, S9.6; no longer S8.3, S8.6
- net 3.3V_SW2: now also S14.3, S14.6; no longer S12.3, S12.6
- net 3.3V_SW3: now also S19.3, S19.6; no longer S16.3, S16.6
- net 3.3V_SW4: now also S24.3, S24.6; no longer S20.3, S20.6
- net 3.3V_SW5: now also S29.3, S29.6; no longer S24.3, S24.6
- net D1: now also S7.1, S7.2; no longer S6.1, S6.2
- net D13/TXO: now also S4.6; no longer B1.RX
- net D13/TXO1: now also S10.6; no longer B2.RX
- net D13/TXO2: now also S15.6; no longer B3.RX
- net D13/TXO3: now also S20.6; no longer B4.RX
- net D13/TXO4: now also S25.6; no longer B5.RX
- net D13/TXO5: now also S30.6; no longer B6.RX
- net D14/RXI: now also S4.3; no longer B1.TX
- net D14/RXI1: now also S10.3; no longer B2.TX
- net D14/RXI2: now also S15.3; no longer B3.TX
- net D14/RXI3: now also S20.3; no longer B4.TX
- net D14/RXI4: now also S25.3; no longer B5.TX
- net D14/RXI5: now also S30.3; no longer B6.TX
- net D2: now also S12.1, S12.2; no longer S10.1, S10.2
- net D3: now also S17.1, S17.2; no longer S14.1, S14.2
- net D4: now also S22.1, S22.2; no longer S18.1, S18.2
- net D5: now also S27.1, S27.2; no longer S22.1, S22.2
- net DIRECT_SELECT1: now also S8.2, S8.5; no longer S7.2, S7.5
- net DIRECT_SELECT2: now also S13.2, S13.5; no longer S11.2, S11.5
- net DIRECT_SELECT3: now also S18.2, S18.5; no longer S15.2, S15.5
- net DIRECT_SELECT4: now also S23.2, S23.5; no longer S19.2, S19.5
- net DIRECT_SELECT5: now also S28.2, S28.5; no longer S23.2, S23.5
- net DIRECT_USB1: now also S8.1, S8.4; no longer S7.1, S7.4
- net DIRECT_USB2: now also S13.1, S13.4; no longer S11.1, S11.4
- net DIRECT_USB3: now also S18.1, S18.4; no longer S15.1, S15.4
- net DIRECT_USB4: now also S23.1, S23.4; no longer S19.1, S19.4
- net DIRECT_USB5: now also S28.1, S28.4; no longer S23.1, S23.4
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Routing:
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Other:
- board text added: "v11"
- board text removed: "1.6mm Thickness"
- board text removed: "1oz Outer Layer 0.5oz Inner Layer JLC0416H-7628 Stackup"
- board text removed: "Four Layer Board"
- board text removed: "Lead Free HASL"
- board text removed: "Material: FR4: TG135-140"
- board text removed: "Red Soldermask"
- board text removed: "White Silk"
- board text removed: "v10"
